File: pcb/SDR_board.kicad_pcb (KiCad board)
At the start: 4 copper layers, 100 x 100 mm, 467 parts, among them J1 USB_B_Mini, J201 Molex 73251-1150 SMA, J301 Molex 73251-1150 SMA, J401 Molex 73251-1150 SMA, J501 Molex 73251-1150 SMA, M3.2 MountingHole_3.2mm_M3_DIN965_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, SW1 SW_Push, U1 AMS1117-3.3, U2 NB3L553, U201 BGA2803, U202 MSi001-Q40, U203 MAX19777AZA+, U204 ADS7883, U205 LMV712-N, U206 MAX19777AZA+, U207 ADS7883, U3 CY7C68013A-56PVX, U301 BGA2803, U302 MSi001-Q40, U303 MAX19777AZA+, U304 ADS7883, U305 LMV712-N, U306 MAX19777AZA+, U307 ADS7883, U401 BGA2803, U402 MSi001-Q40, U403 MAX19777AZA+, U404 ADS7883, U405 LMV712-N, U406 MAX19777AZA+, U407 ADS7883, U5 24LC128, U501 BGA2803, U502 MSi001-Q40, U503 MAX19777AZA+, U504 ADS7883, U505 LMV712-N, U506 MAX19777AZA+, U507 ADS7883, U6 MCP1825S, X1 XO32, X2 XO32

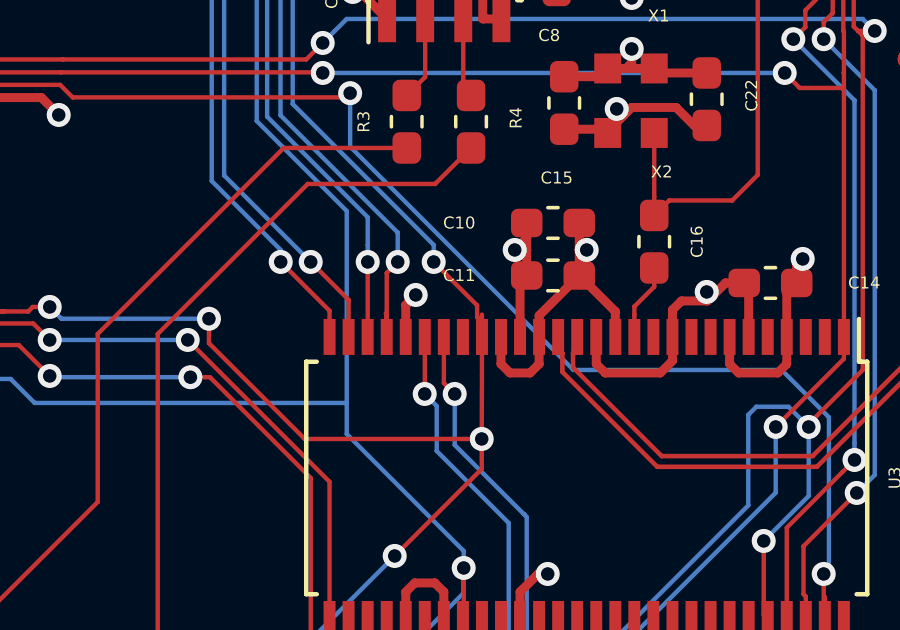
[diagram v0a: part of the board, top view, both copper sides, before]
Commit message: Pulled the reserved pin of fx2lp to GND, per the fx2lp PCB dev guide
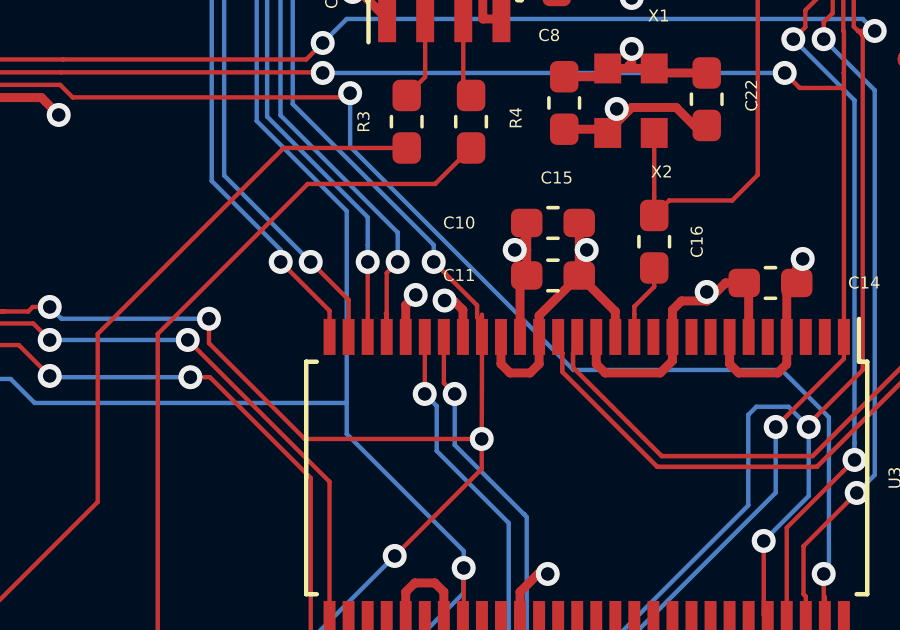
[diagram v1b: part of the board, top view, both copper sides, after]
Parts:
- C13: value 10nF -> 0.1uF
- C222, C223, C322, C323, C422, C423, C522, C523: value 220pF -> 390pF
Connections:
- U3 pad 21: (no net) -> GND
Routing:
- net GND: track 409.1 -> 410.7 mm, vias 201 -> 202
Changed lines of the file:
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@@
     (thickness 1.6)
     (drawings 51)
-    (tracks 4653)
+    (tracks 4657)
     (zones 0)
     (modules 467)
@@
     (pad 20 smd rect (at -4.7 3.4925 270) (size 1.2 0.4) (layers Front_1.Cu F.Paste F.Mask)
       (net 134 ADC_CLK))
-    (pad 21 smd rect (at -4.7 4.1275 270) (size 1.2 0.4) (layers Front_1.Cu F.Paste F.Mask))
+    (pad 21 smd rect (at -4.7 4.1275 270) (size 1.2 0.4) (layers Front_1.Cu F.Paste F.Mask)
+      (net 2 GND))
     (pad 22 smd rect (at -4.7 4.7625 270) (size 1.2 0.4) (layers Front_1.Cu F.Paste F.Mask)
       (net 148 "Net-(R10-Pad2)"))
@@
       (effects (font (size 0.4 0.4) (thickness 0.07)))
     )
-    (fp_text value 10nF (at 0 1.43 180) (layer F.Fab)
+    (fp_text value 0.1uF (at 0 1.43 180) (layer F.Fab)
       (effects (font (size 1 1) (thickness 0.15)))
     )
@@
       (effects (font (size 0.4 0.4) (thickness 0.07)))
     )
-    (fp_text value 220pF (at 0 1.43 225) (layer F.Fab)
+    (fp_text value 390pF (at 0 1.43 225) (layer F.Fab)
       (effects (font (size 1 1) (thickness 0.15)))
     )
@@
       (effects (font (size 0.4 0.4) (thickness 0.07)))
     )
-    (fp_text value 220pF (at 0 1.43 180) (layer F.Fab)
+    (fp_text value 390pF (at 0 1.43 180) (layer F.Fab)
       (effects (font (size 1 1) (thickness 0.15)))
     )
@@
       (effects (font (size 0.4 0.4) (thickness 0.07)))
     )
-    (fp_text value 220pF (at 0 1.43 225) (layer F.Fab)
+    (fp_text value 390pF (at 0 1.43 225) (layer F.Fab)
       (effects (font (size 1 1) (thickness 0.15)))
     )
@@
       (effects (font (size 0.4 0.4) (thickness 0.07)))
     )
-    (fp_text value 220pF (at 0 1.43 180) (layer F.Fab)
+    (fp_text value 390pF (at 0 1.43 180) (layer F.Fab)
       (effects (font (size 1 1) (thickness 0.15)))
     )
@@
       (effects (font (size 0.4 0.4) (thickness 0.07)))
     )
-    (fp_text value 220pF (at 0 1.43 225) (layer F.Fab)
+    (fp_text value 390pF (at 0 1.43 225) (layer F.Fab)
       (effects (font (size 1 1) (thickness 0.15)))
     )
@@
       (effects (font (size 0.4 0.4) (thickness 0.07)))
     )
-    (fp_text value 220pF (at 0 1.43 180) (layer F.Fab)
+    (fp_text value 390pF (at 0 1.43 180) (layer F.Fab)
       (effects (font (size 1 1) (thickness 0.15)))
     )
@@
       (effects (font (size 0.4 0.4) (thickness 0.07)))
     )
-    (fp_text value 220pF (at 0 1.43 225) (layer F.Fab)
+    (fp_text value 390pF (at 0 1.43 225) (layer F.Fab)
       (effects (font (size 1 1) (thickness 0.15)))
     )
@@
       (effects (font (size 0.4 0.4) (thickness 0.07)))
     )
-    (fp_text value 220pF (at 0 1.43 180) (layer F.Fab)
+    (fp_text value 390pF (at 0 1.43 180) (layer F.Fab)
       (effects (font (size 1 1) (thickness 0.15)))
     )
@@
   (segment (start 63.578595 105.428595) (end 63.578595 105.671405) (width 0.3) (layer Front_1.Cu) (net 2))
   (via (at 117.5 38.9) (size 0.8) (drill 0.45) (layers Front_1.Cu Back_4.Cu) (net 2))
+  (via (at 101.562149 79.886198) (size 0.8) (drill 0.45) (layers Front_1.Cu Back_4.Cu) (net 2))
+  (segment (start 101.858698 79.886198) (end 101.562149 79.886198) (width 0.3) (layer Front_1.Cu) (net 2))
+  (segment (start 102.1725 81.1) (end 102.1725 80.2) (width 0.3) (layer Front_1.Cu) (net 2))
+  (segment (start 102.1725 80.2) (end 101.858698 79.886198) (width 0.3) (layer Front_1.Cu) (net 2))
   (segment (start 119.225 62.7) (end 117.5 62.7) (width 0.3) (layer Front_1.Cu) (net 3))
   (segment (start 121.5 64.975) (end 119.225 62.7) (width 0.3) (layer Front_1.Cu) (net 3))
